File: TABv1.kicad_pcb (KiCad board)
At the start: 4 copper layers, 90 x 45 mm, 120 parts, among them IC1 TPS630702RNMR, J10 Conn_02x03_Odd_Even, J11 Conn_01x06_Pin, J5 Conn_02x08_Odd_Even, J6 Conn_02x08_Odd_Even, J7 503398-1892, J8 1053141104, J9 Conn_02x03_Odd_Even, Q1 MJD44H11T4G, Q10 PJM09P30DF, Q11 PJM09P30DF, Q12 PJM09P30DF, Q2 DMN2040U, Q3 DMN2040U, Q4 BC817-25,215, Q5 DMN2040U, Q6 DMN2040U, Q7 DMN2040U, SW1 BOOTSEL, SW2 RESET, U1 RP2350B-QFN80, U11 LPS22DF, U2 W25Q128JVS, U4 LSM6DSV80XTR, U5 LSM6DSV80XTR, U7 LM334M, U8 LIS2MDL, Y1 12MHz

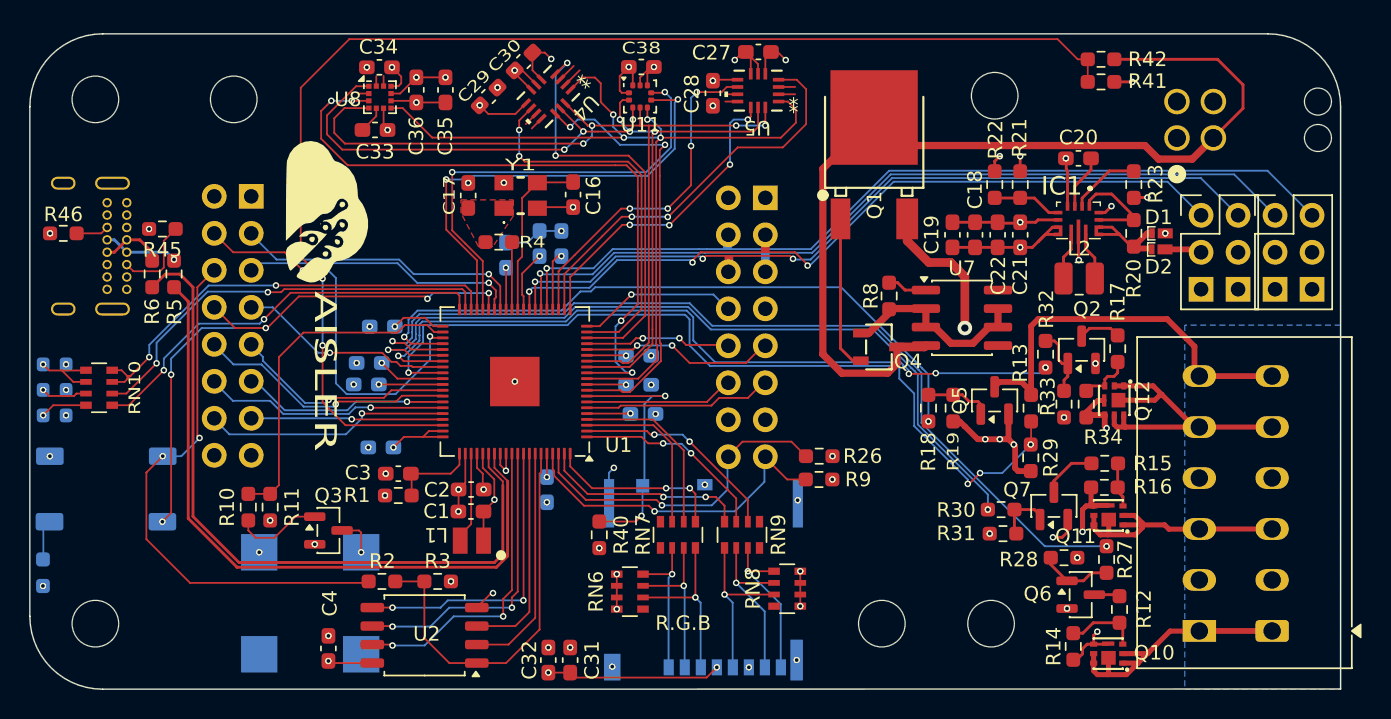
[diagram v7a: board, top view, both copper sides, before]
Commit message: rerouting 0.15mm piste
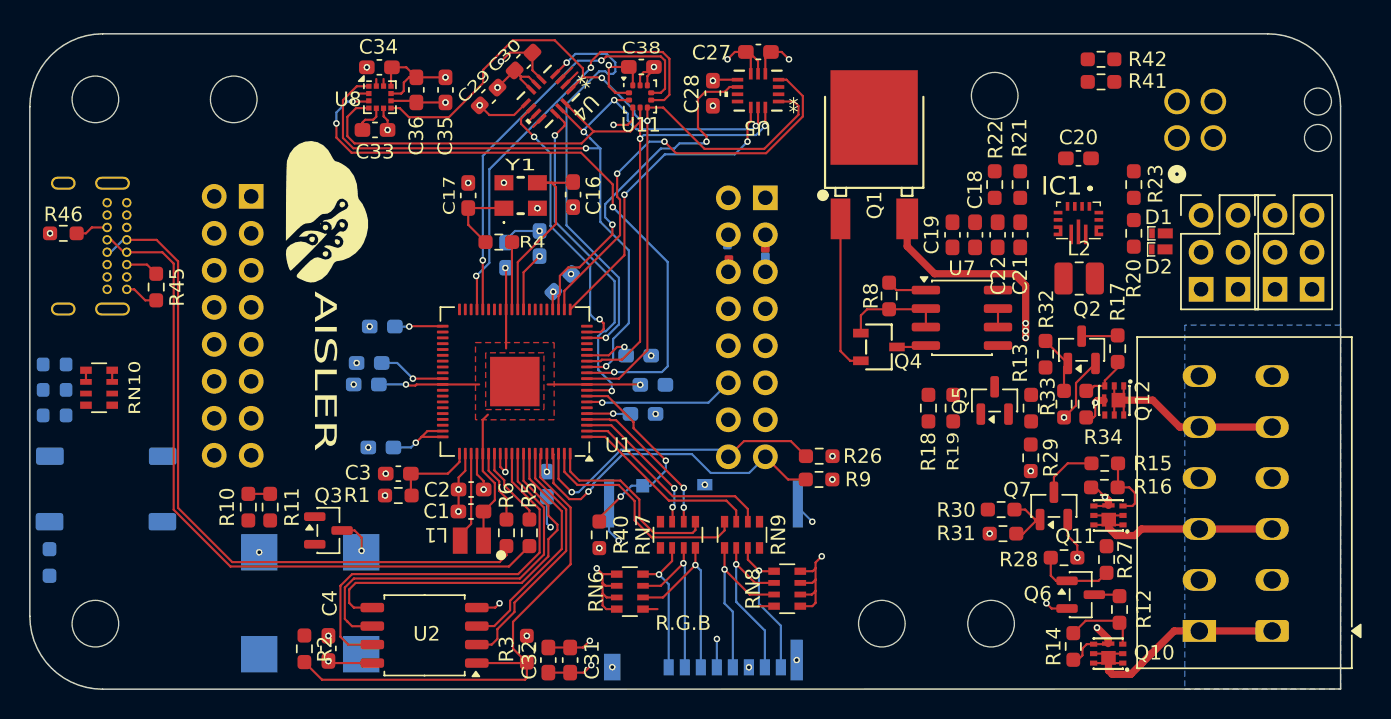
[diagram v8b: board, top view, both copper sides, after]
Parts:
- moved R5 30.2 mm to (106.8, 67.8), turned to -90 degrees
- moved R6 30.1 mm to (105.2, 67.8), turned to -90 degrees
- moved R3 7.69 mm to (106.6, 75.8), turned to -90 degrees
- moved R2 7.05 mm to (91.3, 75.7), turned to -90 degrees
- moved R45 4.01 mm to (81.2, 50.9), turned to -90 degrees
- moved C8 2.70 mm to (109.0, 50.6), turned to -135 degrees
- moved C15 0.98 mm to (115.3, 57.6)
- moved R7 0.83 mm to (73.8, 69.8)
- moved C6 0.38 mm to (108.0, 64.4)
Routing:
- net /BATT_SENSE: track 88.7 -> 0.00 mm, vias 2 -> 0
- net +BATT: track 68.6 -> 2.02 mm
- net /PYRO_FIRE_1: track 63.5 -> 0.00 mm, vias 2 -> 0
- net /PWM1: track 60.5 -> 0.00 mm, vias 1 -> 0
- net /PYRO_SENSE: track 58.6 -> 0.00 mm, vias 4 -> 0
- net /PWM2: track 57.0 -> 0.00 mm, vias 1 -> 0
- net /PYRO_FIRE_2: track 55.3 -> 0.00 mm, vias 2 -> 0
- net /PWM3: track 54.5 -> 0.00 mm, vias 3 -> 0
- net /PYRO_FIRE_3: track 52.7 -> 0.00 mm, vias 4 -> 0
- net /PWM4: track 52.5 -> 0.00 mm, vias 3 -> 0
- net /PYRO_ENABLE: track 46.5 -> 0.00 mm, vias 2 -> 0
- net Net-(U1-USB_DM): track 49.4 -> 5.03 mm
- net D+: track 5.16 -> 48.8 mm, vias 1 -> 0
- net D-: track 4.38 -> 47.7 mm
- net Net-(U1-USB_DP): track 47.3 -> 5.52 mm
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- added copper zone on F.Cu, net +1V1
- removed copper zone on In2.Cu, net +1V1
- removed copper zone on F.Cu, net Net-(C17-Pad2)
